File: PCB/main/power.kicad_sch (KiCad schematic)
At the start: 28 parts, among them IC1 LM358DR2G, IC2 ap2007, IC3 TP4056-42-ESOP8, IC4 LM3940IMP-3.3_NOPB, Q1 AO3401A

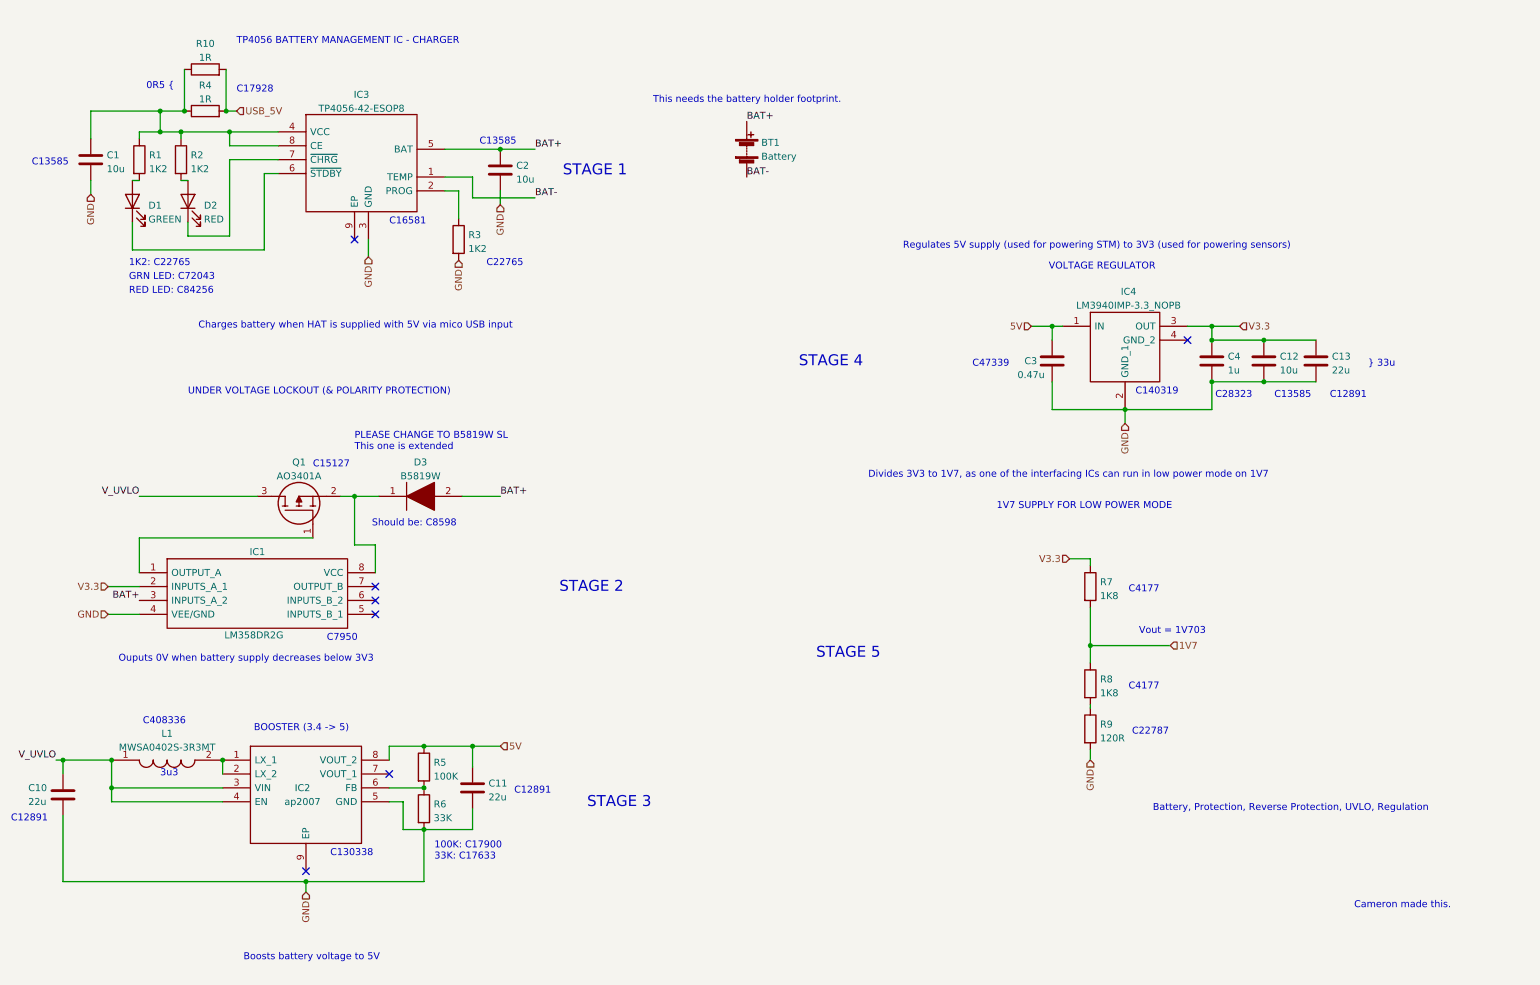
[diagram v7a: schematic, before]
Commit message: Updated all footprints of components
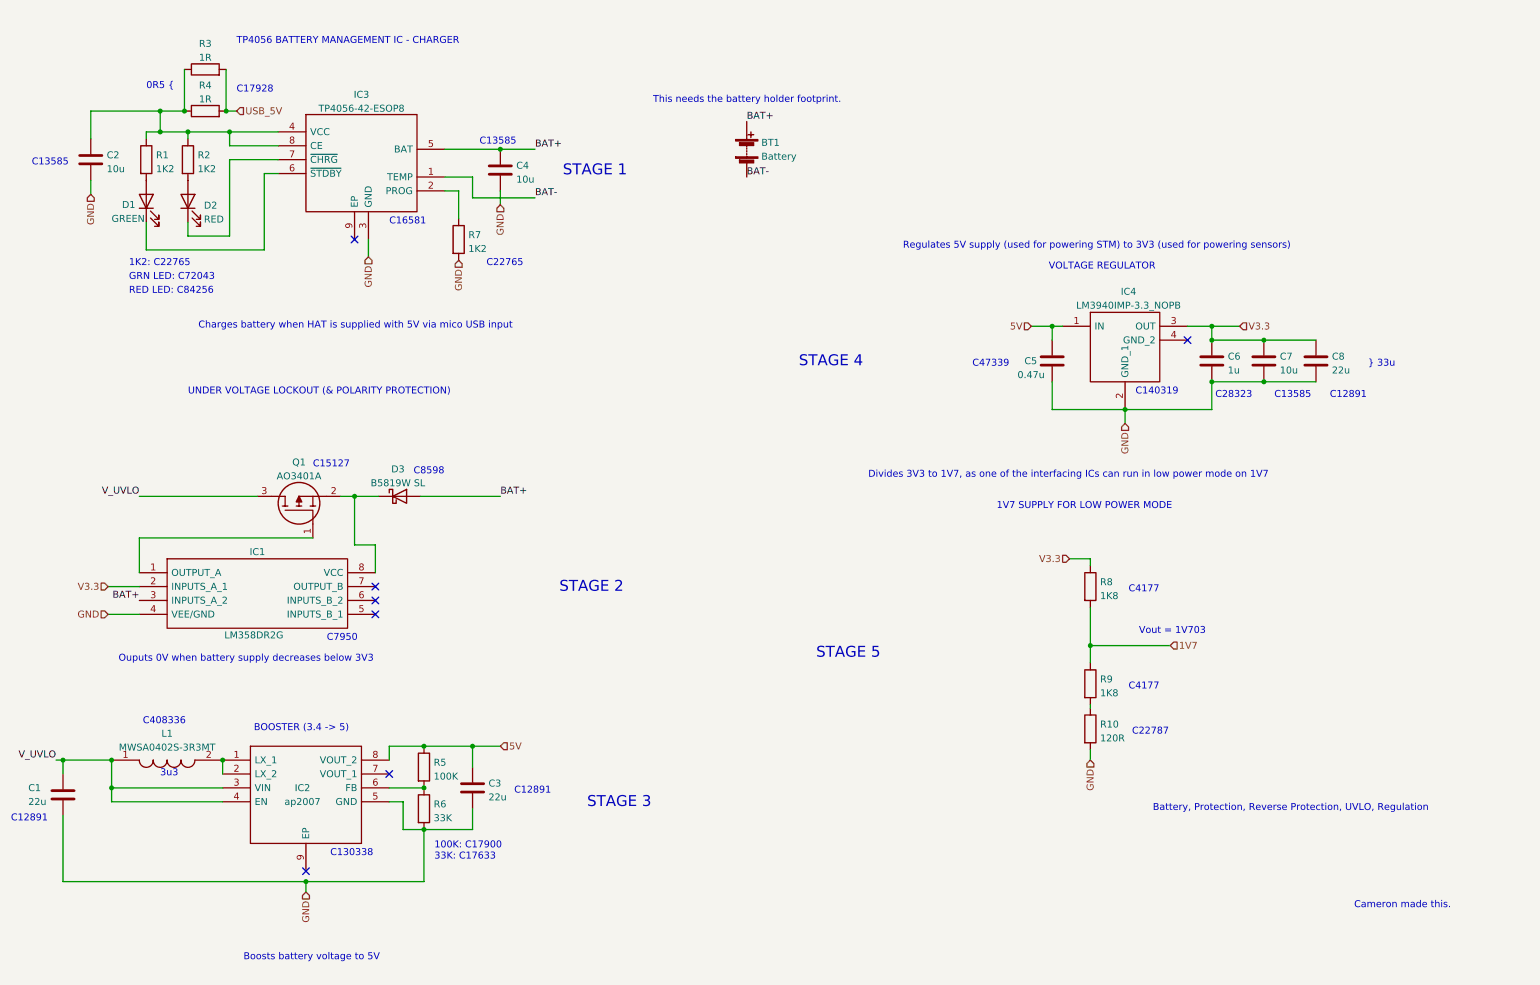
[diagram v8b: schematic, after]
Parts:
- removed D3: B5819W, symbol B5819W:B5819W
- added D3: B5819W SL, EEE3088F_Footprints:SOD-123_L2.7-W1.6-LS3.7-RD-1, symbol Device:D_Schottky
- BT1: footprint (none) -> EEE3088F_Footprints:18650_Holder_THT
- C1: renamed from C10; footprint (none) -> EEE3088F_Footprints:CAPC3216X180N
- C2: renamed from C1; footprint (none) -> EEE3088F_Footprints:CAPC3216X180N
- C3: renamed from C11; footprint (none) -> EEE3088F_Footprints:CAPC3216X180N
- C4: renamed from C2; footprint (none) -> EEE3088F_Footprints:CAPC3216X180N
- C5: renamed from C3; footprint (none) -> EEE3088F_Footprints:CAPC1005X55N
- C6: renamed from C4; footprint (none) -> EEE3088F_Footprints:CAPC1608X90N
- C7: renamed from C12; footprint (none) -> EEE3088F_Footprints:CAPC3216X180N
- C8: renamed from C13; footprint (none) -> EEE3088F_Footprints:CAPC3216X180N
- D1: footprint (none) -> EEE3088F_Footprints:LEDC1608X50N
- D2: footprint (none) -> EEE3088F_Footprints:LED0805-RD_RED
- IC1: footprint (none) -> EEE3088F_Footprints:SOIC127P600X175-8N
- IC2, IC3: footprint (none) -> EEE3088F_Footprints:SOIC127P600X175-9N
- IC4: footprint (none) -> EEE3088F_Footprints:SOT230P700X180-4N
- L1: footprint (none) -> EEE3088F_Footprints:INDPM4442X200N
- Q1: footprint (none) -> EEE3088F_Footprints:SOT95P280X125-3N
- R1, R2: footprint (none) -> EEE3088F_Footprints:RESC1608X55N
- R10: renamed from R9; footprint (none) -> EEE3088F_Footprints:R0603
- R3: renamed from R10; footprint (none) -> EEE3088F_Footprints:R1206
- R4: footprint (none) -> EEE3088F_Footprints:R1206
- R5: footprint (none) -> EEE3088F_Footprints:RESC3116X65N
- R6: footprint (none) -> EEE3088F_Footprints:RESC2013X65N
- R7: renamed from R3; footprint (none) -> EEE3088F_Footprints:RESC1608X55N
- R8: renamed from R7; footprint (none) -> EEE3088F_Footprints:RESC1608X55N
- R9: renamed from R8; footprint (none) -> EEE3088F_Footprints:RESC1608X55N
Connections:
- net BAT+: now also D3.2 (A)
- net at IC1.8 (VCC), Q1.2: now also D3.1 (K)
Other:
- note added: "C8598"
- note removed: "PLEASE CHANGE TO B5819W SL This one is extended"
- note removed: "Should be: C8598"
- moved on the sheet: D1, R1, R2
